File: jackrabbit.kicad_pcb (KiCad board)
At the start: 2 copper layers, 45.1 x 29.2 mm, 62 parts, among them J1 USB_C, J2 PinHeader_2.54mm_02x10, J3 PinHeader_2.54mm_02x04, J4 PinHeader_2.54mm_02x04, J5 PinHeader_2.54mm_01x04, J6 PinHeader_2.54mm_01x03, SW1 SW_Push, SW2 SW_Push, U1 MIC5319-3.3YD5, U2 74LVX245, U3 W25Q16JVSNIQ, U4 RP2040, U5 74LVX245, Y1 ECS-120-18-33-JGN

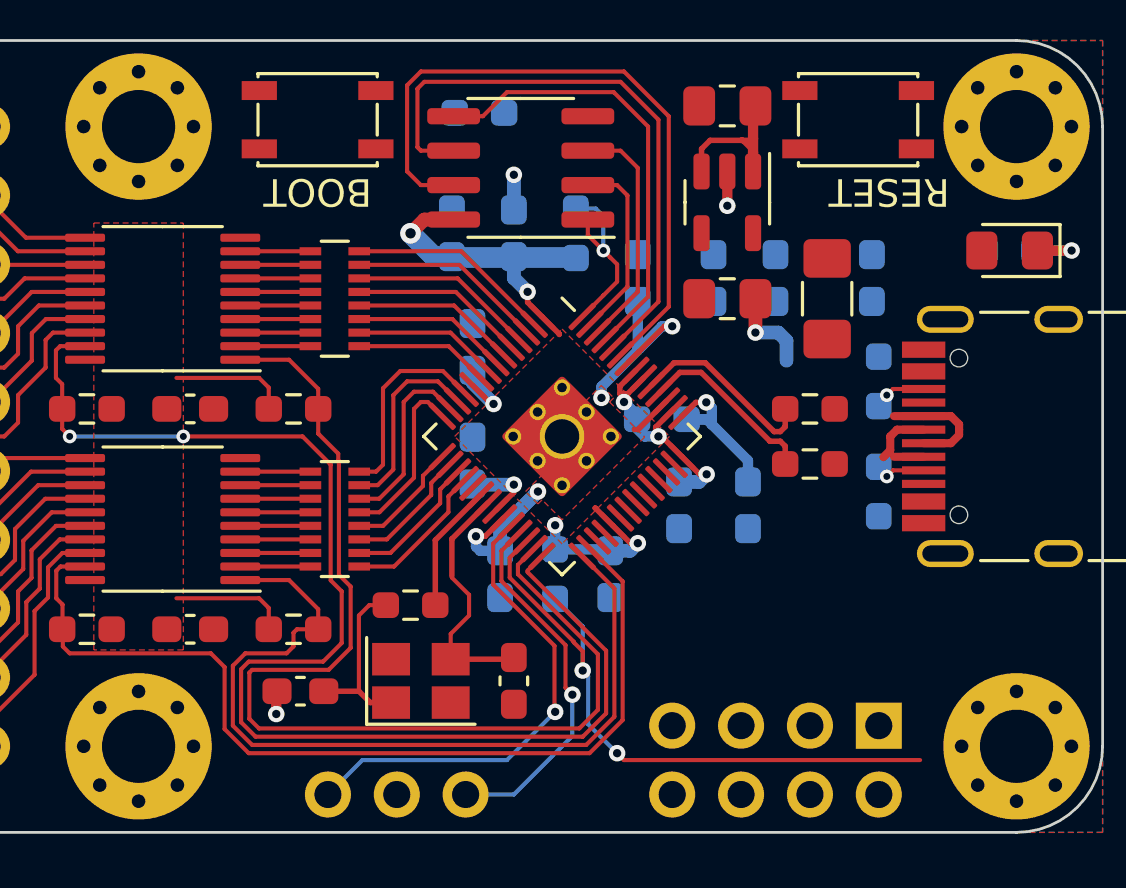
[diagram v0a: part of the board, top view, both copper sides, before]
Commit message: Continue layout; add labels for digital connector
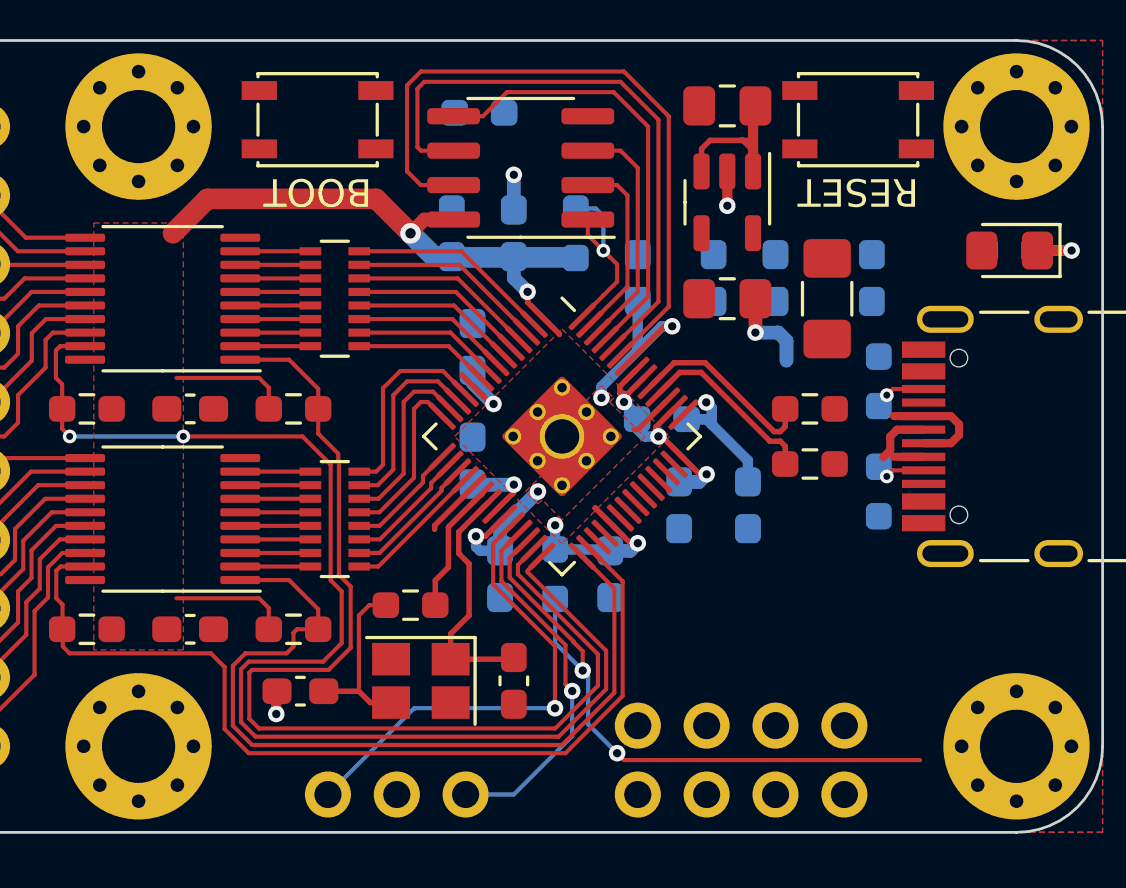
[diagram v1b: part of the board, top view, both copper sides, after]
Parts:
- added kibuzzard-62E75BC5: G***, kibuzzard-62E75BC5, B.Cu at (117.9, 125.9)
- added kibuzzard-62E75BC5: G***, kibuzzard-62E75BC5, B.Cu at (117.9, 110.3)
- moved J3 1.27 mm to (144.7, 128.8)
- turned Y1 to 180 degrees
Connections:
- Y1 pad 1: Net-(C17-Pad2) -> Net-(C18-Pad2)
- Y1 pad 3: Net-(C18-Pad2) -> Net-(C17-Pad2)
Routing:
- net +3V3: track 44.1 -> 53.9 mm
- net GND: track 4.86 -> 7.00 mm
- net Net-(J1-PadB5): track 0.00 -> 1.45 mm, vias 0 -> 1
- net Net-(J1-PadA5): track 1.45 -> 0.00 mm, vias 1 -> 0
- net /~{OE_A}: track 48.8 -> 48.3 mm
- net /~{DIR_OUT_A}: track 39.9 -> 39.4 mm
- net /~{OE_B}: track 35.0 -> 34.5 mm
- net /~{DIR_OUT_B}: track 31.5 -> 31.0 mm
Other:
- board text added: "0"
- board text added: "1"
- board text added: "10"
- board text added: "11"
- board text added: "12"
- board text added: "13"
- board text added: "14"
- board text added: "15"
- board text added: "2"
- board text added: "3"
- board text added: "4"
- board text added: "5"
- board text added: "6"
- board text added: "7"
- board text added: "8"
- board text added: "9"

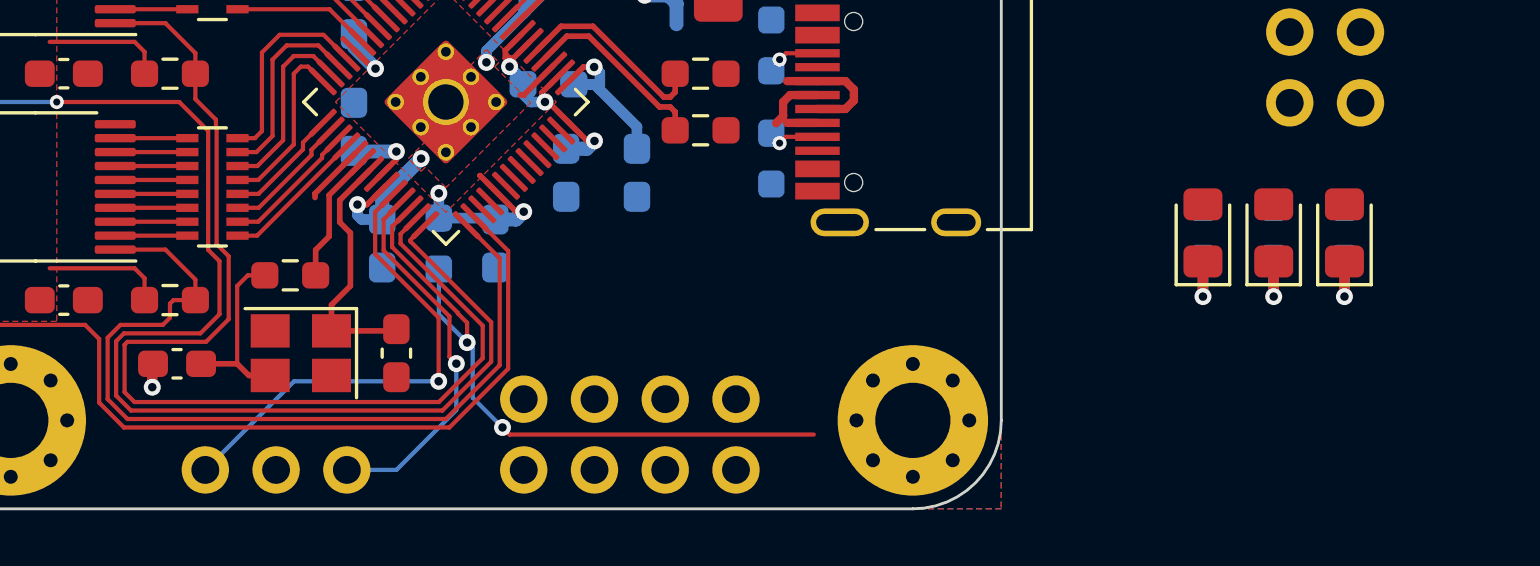
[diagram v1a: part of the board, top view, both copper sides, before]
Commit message: Add logos and connector labels
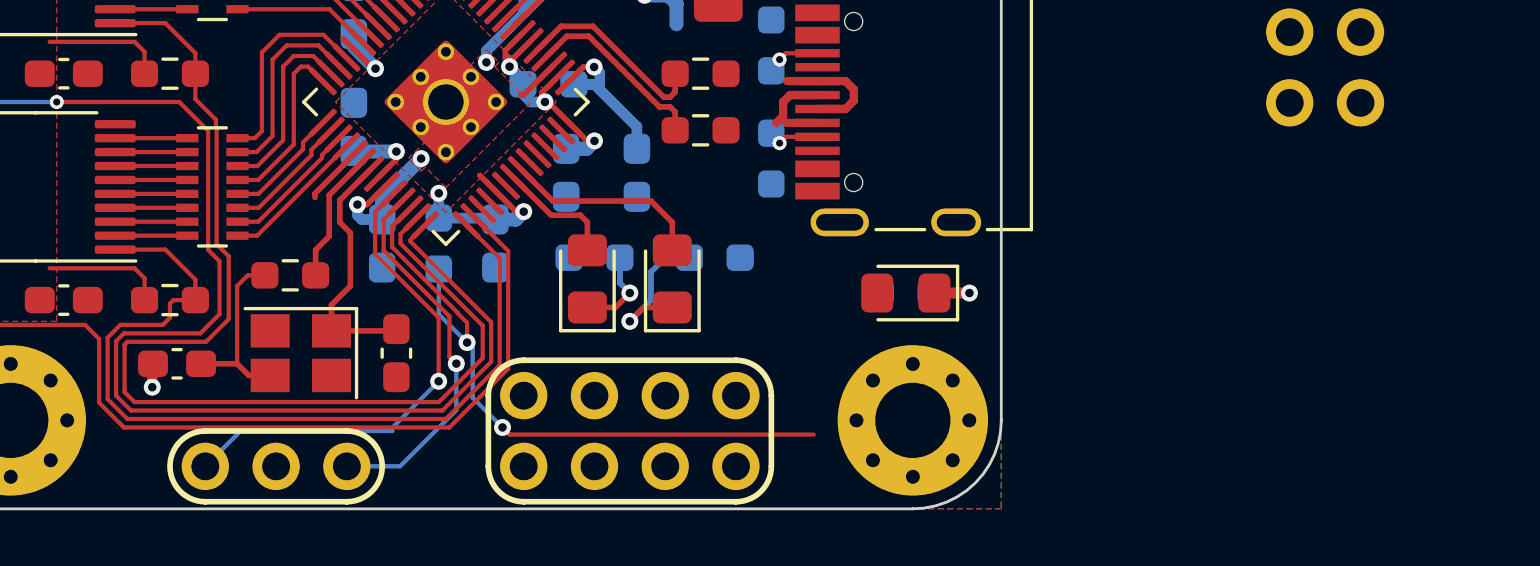
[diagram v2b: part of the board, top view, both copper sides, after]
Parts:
- added kibuzzard-62E7A97F: G***, kibuzzard-62E7A97F, B.Cu at (125.1, 115.8)
- added kibuzzard-62E7AE0F: G***, kibuzzard-62E7AE0F, B.Cu at (128.1, 128.0)
- moved D2 22.2 mm to (139.3, 124.4)
- moved R15 21.9 mm to (139.6, 123.7), turned to 180 degrees
- moved D3 21.7 mm to (142.4, 124.4)
- moved R16 20.1 mm to (143.9, 123.7), turned to 0 degrees
- moved D4 15.9 mm to (150.7, 124.9), turned to 180 degrees
- moved R17 15.9 mm to (150.7, 124.9), turned to 180 degrees
- moved J3 0.13 mm to (144.7, 128.6)
- moved J6 0.13 mm to (125.6, 131.2)
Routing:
- net /LEDB: track 0.00 -> 7.19 mm
- net /LEDA: track 0.00 -> 4.31 mm
- net Net-(D3-Pad1): track 2.63 -> 5.41 mm
- net Net-(D2-Pad1): track 2.63 -> 3.16 mm
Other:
- board text added: "A0"
- board text added: "A1"
- board text added: "A2"
- board text added: "A3"
- board text added: "SWCLK"
- board text added: "SWDIO"

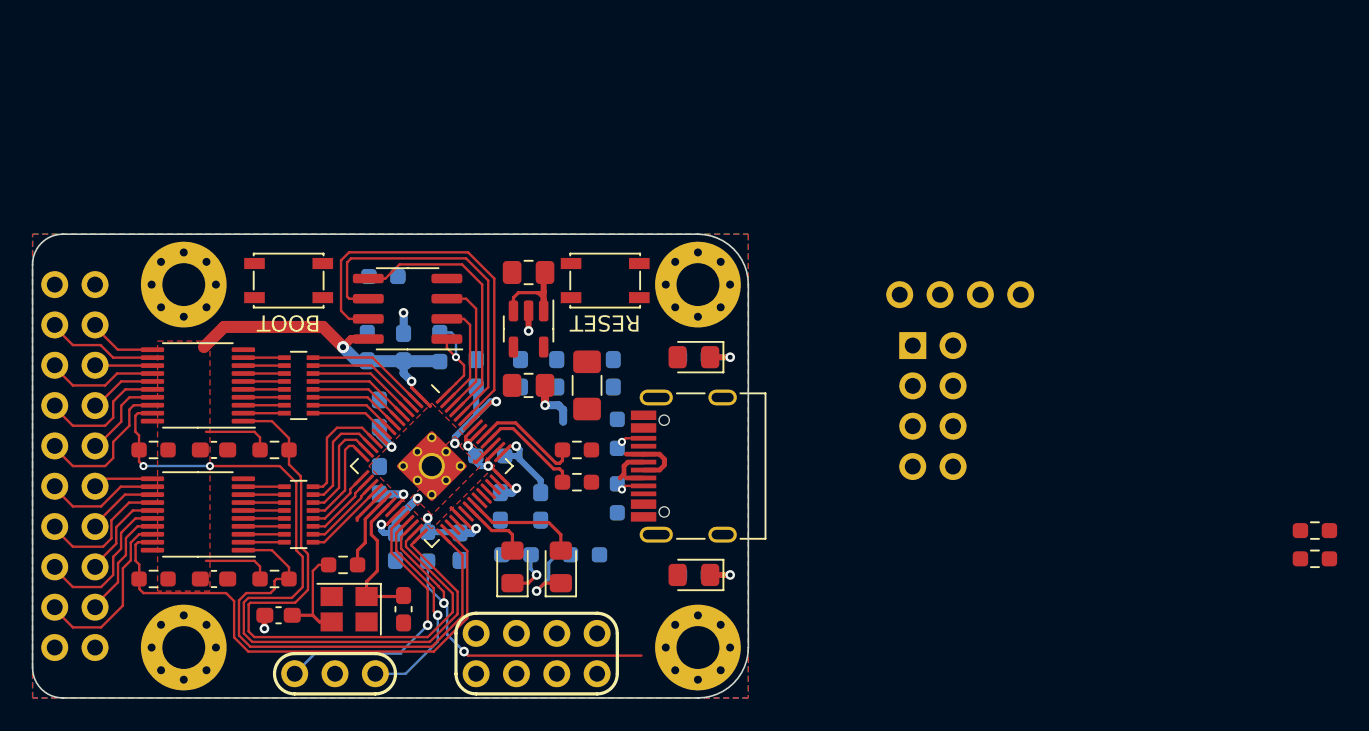
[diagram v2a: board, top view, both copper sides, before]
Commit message: Connect bootsel button to a GPIO; remove connectors for which we have no room
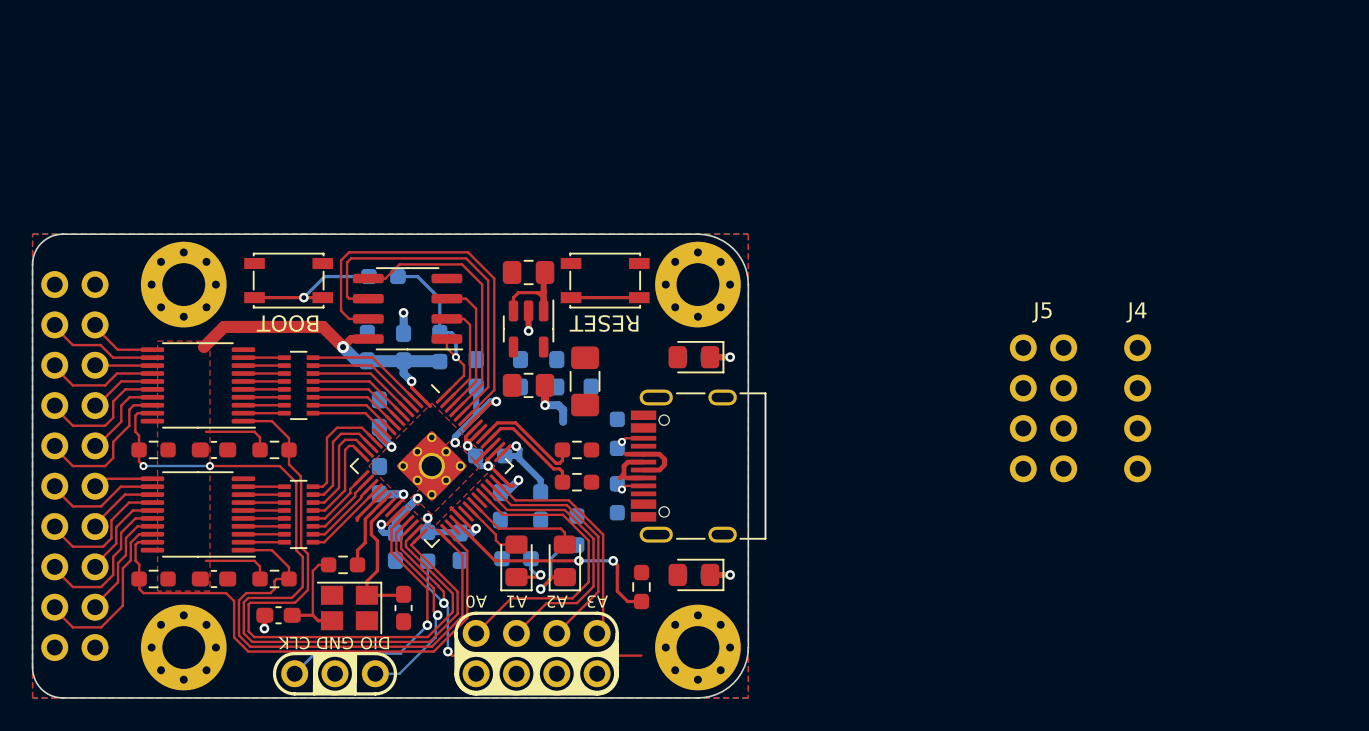
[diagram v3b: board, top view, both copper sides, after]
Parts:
- removed the R8 at (189.9, 122.2)
- J4: value PinHeader_2.54mm_02x04 -> PinHeader_2.54mm_01x04; footprint jackrabbit:PinHeader_2x04_P2.54mm_NoSilk -> jackrabbit:PinHeader_1x04_P2.54mm_NoSilk
- J5: value PinHeader_2.54mm_01x04 -> PinHeader_2.54mm_02x04; footprint jackrabbit:PinHeader_1x04_P2.54mm_NoSilk -> jackrabbit:PinHeader_2x04_P2.54mm_NoSilk
- R11: renamed from R7; value 100 -> 1k
- R6: value DNP -> 10k
- moved R11 42.5 mm to (147.4, 125.7), turned to 90 degrees
- moved J4 14.2 mm to (178.7, 110.6)
- moved J5 8.47 mm to (171.5, 110.6), turned to 0 degrees
- moved R17 1.61 mm to (143.4, 122.2), turned to 90 degrees
- moved C1 1.40 mm to (144.3, 112.2)
- moved D2 0.46 mm to (139.6, 124.1)
- moved D3 0.46 mm to (142.6, 124.1)
- moved F1 0.28 mm to (143.9, 112.8)
- moved R16 0.25 mm to (139.6, 123.9)
- moved kibuzzard-62E7AE0F 0.13 mm to (128.1, 127.9)
- moved Y1 0.08 mm to (129.1, 127.0)
- moved C18 0.08 mm to (132.5, 127.0)
- renumbered J6 to J4, R11 to R10, R19 to R14, R14 to R15, R15 to R16, R16 to R17, R17 to R18, R9 to R7, R18 to R8, R10 to R9
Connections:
- J4 pad 1: +5V -> /RX
- J4 pad 2: +5V -> /TX
- J4 pad 3: +3V3 -> GND
- J5 pad 1: /RX -> +5V
- J5 pad 2: /TX -> +5V
- J5 pad 3: GND -> +3V3
- R11 pad 1: Net-(R7-Pad1) -> Net-(R11-Pad1)
- R11 pad 2: /TX -> /~{USB_BOOT}
- U4 pad 31: Net-(R7-Pad1) -> unconnected-(U4-Pad31)
- U4 pad 32: Net-(R8-Pad1) -> Net-(R11-Pad1)
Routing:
- net /ADC0: track 0.00 -> 18.8 mm
- net /ADC1: track 0.00 -> 16.9 mm
- net /ADC2: track 0.00 -> 15.1 mm
- net Net-(R11-Pad1): track 0.00 -> 14.6 mm, vias 0 -> 2
- net /ADC3: track 0.00 -> 14.4 mm
- net /~{USB_BOOT}: track 0.00 -> 8.95 mm, vias 0 -> 1
- net /QSPI_SS: track 7.73 -> 13.1 mm
- net /~{RESET}: track 24.1 -> 29.0 mm
- net +3V3: track 53.9 -> 54.5 mm
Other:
- board text added: "CLK"
- board text added: "DIO"
- board text added: "GND"

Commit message: Continue layout; prettify digital connector labels
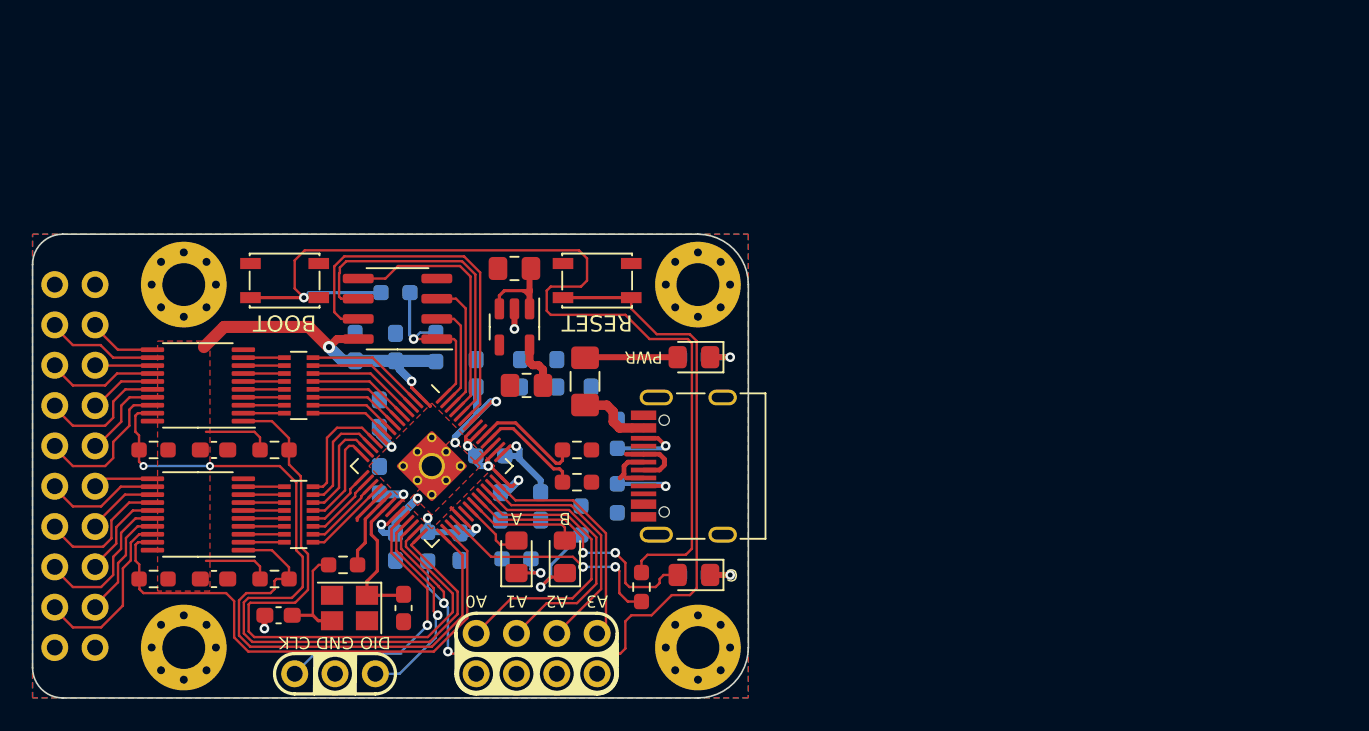
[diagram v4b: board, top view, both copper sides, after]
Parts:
- removed the J4 at (178.7, 110.6)
- removed J5: PinHeader_2.54mm_02x04, jackrabbit:PinHeader_2x04_P2.54mm_NoSilk
- removed kibuzzard-62E75BC5 (x2): G***, kibuzzard-62E75BC5
- added kibuzzard-62E8C5F1: G***, kibuzzard-62E8C5F1, B.Cu at (118.6, 110.3)
- added kibuzzard-62E8C5F1: G***, kibuzzard-62E8C5F1, B.Cu at (118.7, 125.9)
- moved R9 1.27 mm to (131.9, 107.2)
- moved C2 0.92 mm to (139.4, 105.6)
- moved U1 0.90 mm to (139.4, 109.3)
- moved C15 0.76 mm to (129.4, 110.6)
- moved R17 0.68 mm to (143.6, 121.5)
- moved U3 0.63 mm to (132.1, 108.2)
- moved C9 0.51 mm to (131.9, 110.6)
- moved SW2 0.51 mm to (144.7, 106.4)
- moved D2 0.25 mm to (139.6, 123.8)
- moved D3 0.25 mm to (142.6, 123.8)
- moved R6 0.25 mm to (134.5, 110.6)
- moved SW1 0.25 mm to (125.0, 106.4)
- moved C3 0.13 mm to (140.2, 113.0)
- turned R1 to 90 degrees
- turned R2 to -90 degrees
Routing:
- net /~{USB_BOOT}: track 8.95 -> 63.4 mm
- net /~{RESET}: track 29.0 -> 56.3 mm
- net /LEDC: track 0.00 -> 16.5 mm, vias 0 -> 2
- net +5V: track 6.01 -> 12.1 mm
- net VUSB: track 0.00 -> 4.93 mm
- net Net-(J1-PadA5): track 0.00 -> 4.51 mm, vias 0 -> 1
- net Net-(J1-PadB5): track 1.45 -> 4.70 mm
- net GND: track 7.00 -> 4.26 mm, vias 4 -> 2
- net /QSPI_SS: track 13.1 -> 11.1 mm
- net /QSPI_SD0: track 17.3 -> 16.5 mm
- net /QSPI_SD3: track 24.4 -> 23.9 mm
- net +3V3: vias 10 -> 9
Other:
- board text added: "A"
- board text added: "B"
- board text added: "C"
- board text added: "PWR"

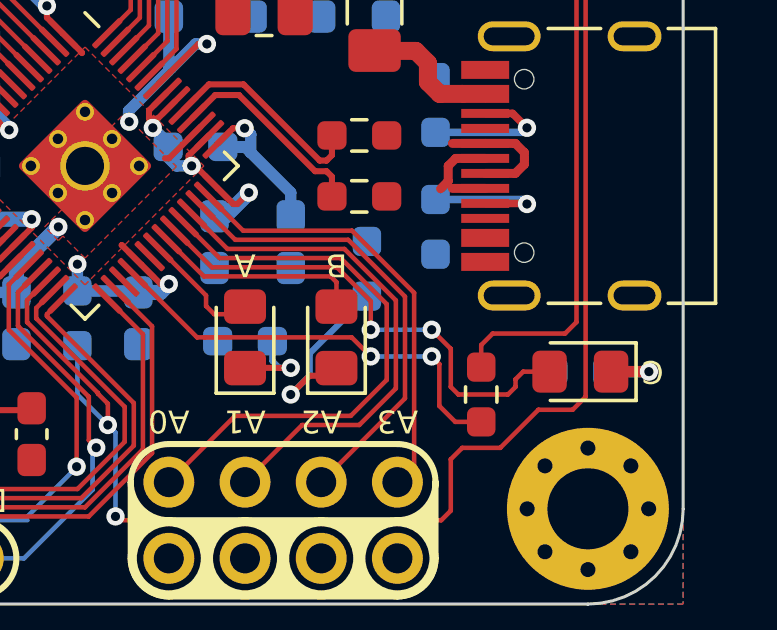
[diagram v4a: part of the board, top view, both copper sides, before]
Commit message: Flip LED labels to make 'A" the one by the USB connector
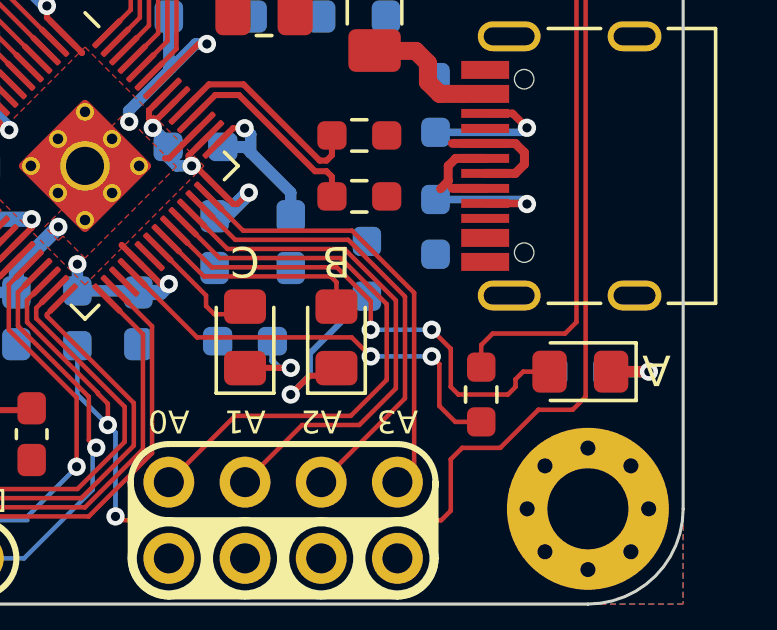
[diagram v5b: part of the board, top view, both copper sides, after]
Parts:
- moved kibuzzard-62E7A97F 0.13 mm to (125.0, 115.8)
- renumbered D4 to D2, D2 to D4
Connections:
- D2 pad 2: /LEDC -> /LEDA
- D4 pad 2: /LEDA -> /LEDC
- U4 pad 35: /LEDA -> /LEDC
- U4 pad 37: /LEDC -> /LEDA
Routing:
- net /LEDC: track 16.5 -> 4.02 mm, vias 2 -> 0
- net /LEDA: track 4.02 -> 16.5 mm, vias 0 -> 2
